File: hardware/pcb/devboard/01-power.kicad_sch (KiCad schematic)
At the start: 42 parts, among them J1 BATTERIE JST-PH, J2 BOUTON contact JST-PH, J3 BOUTON LED JST-PH, Q1 AO3401A, Q2 2N7002, Q3 2N7002, SW1 QON, U2 BQ25896RTW, U3 TPS63001DRCR, U4 TPS61023DRL

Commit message: feat(pcb): cost-optimize the dev board for JLCPCB
- shrink the outline to 99 x 45 mm and recenter MH2/MH4, keeping every
  dimension under 100 mm to dodge the large-board engineering fee
- reshape the In2.Cu +5V plane, restore the GND_surface pour, refill zones
- widen the main VBUS run to 1.2 mm, clearing the G2 thermal warning
- mark J1/J2/J3/J13 (JST-PH) and SW1 DNP: hand-soldered, so the board is
  all-SMD and skips the through-hole wave-solder fixture
- move R1/R10/R11/R26/R27 to Basic 0603 (150R/56k/7.5k), dropping three
  extended feeders; values and the 5V feedback ratio preserved
- swap D1 to the promotional SMF5.0A C19077497 (identical part, fee waived)
- gen_fab: J13 takes no JLCPCB rotation correction (verified in preview)

Co-Authored-By: Claude Opus 4.8 <noreply@anthropic.com>
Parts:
- D1: LCSC C284108 -> C19077497
- J1, J2, J3, SW1: now not fitted
- R1: footprint Resistor_SMD:R_0402_1005Metric -> Resistor_SMD:R_0603_1608Metric; LCSC C25082 -> C22808; MPN 0402WGF1500TCE -> 0603WAF1500T5E
- R10: footprint Resistor_SMD:R_0402_1005Metric -> Resistor_SMD:R_0603_1608Metric; LCSC C25796 -> C23206; MPN 0402WGF5602TCE -> 0603WAF5602T5E
- R11: footprint Resistor_SMD:R_0402_1005Metric -> Resistor_SMD:R_0603_1608Metric; LCSC C25918 -> C23234; MPN 0402WGF7501TCE -> 0603WAF7501T5E
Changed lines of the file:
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@@
 			)
 		)
-		(property "Footprint" "Resistor_SMD:R_0402_1005Metric"
+		(property "Footprint" "Resistor_SMD:R_0603_1608Metric"
 			(at 768.35 43.18000000000001 0)
 			(effects
@@
 			(hide yes)
 		)
-		(property "LCSC" "C25082"
+		(property "LCSC" "C22808"
 			(at 768.35 35.56 0)
 			(effects
@@
 			(hide yes)
 		)
-		(property "MPN" "0402WGF1500TCE"
+		(property "MPN" "0603WAF1500T5E"
 			(at 768.35 33.02000000000001 0)
 			(effects
@@
 		(in_bom yes)
 		(on_board yes)
-		(dnp no)
+		(dnp yes)
 		(fields_autoplaced yes)
 		(property "Reference" "SW1"
@@
 			(hide yes)
 		)
-		(property "LCSC" "C284108"
+		(property "LCSC" "C19077497"
 			(at 229.87 107.94999999999999 0)
 			(effects
@@
 		(in_bom yes)
 		(on_board yes)
-		(dnp no)
+		(dnp yes)
 		(fields_autoplaced yes)
 		(property "Reference" "J1"
@@
 			)
 		)
-		(property "Footprint" "Resistor_SMD:R_0402_1005Metric"
+		(property "Footprint" "Resistor_SMD:R_0603_1608Metric"
 			(at 63.5 180.34 0)
 			(effects
@@
 			(hide yes)
 		)
-		(property "LCSC" "C25796"
+		(property "LCSC" "C23206"
 			(at 63.5 172.72000000000003 0)
 			(effects
@@
 			(hide yes)
 		)
-		(property "MPN" "0402WGF5602TCE"
+		(property "MPN" "0603WAF5602T5E"
 			(at 63.5 170.18 0)
 			(effects
@@
 			)
 		)
-		(property "Footprint" "Resistor_SMD:R_0402_1005Metric"
+		(property "Footprint" "Resistor_SMD:R_0603_1608Metric"
 			(at 139.7 180.34 0)
 			(effects
@@
 			(hide yes)
 		)
-		(property "LCSC" "C25918"
+		(property "LCSC" "C23234"
 			(at 139.7 172.72000000000003 0)
 			(effects
@@
 			(hide yes)
 		)
-		(property "MPN" "0402WGF7501TCE"
+		(property "MPN" "0603WAF7501T5E"
 			(at 139.7 170.18 0)
 			(effects
@@
 		(in_bom yes)
 		(on_board yes)
-		(dnp no)
+		(dnp yes)
 		(fields_autoplaced yes)
 		(property "Reference" "J2"
@@
 		(in_bom yes)
 		(on_board yes)
-		(dnp no)
+		(dnp yes)
 		(fields_autoplaced yes)
 		(property "Reference" "J3"

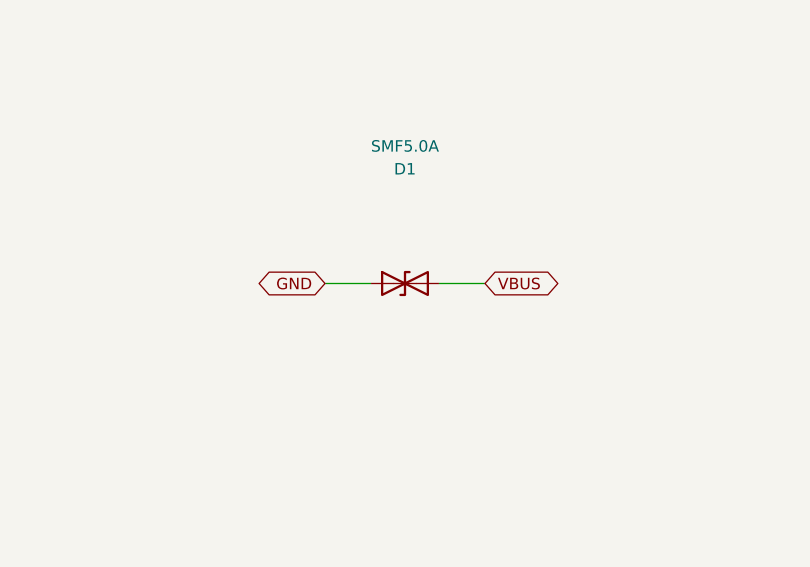
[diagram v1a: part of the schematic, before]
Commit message: fix(pcb): turn the VBUS TVS the right way round on both boards
D1 (SMF5.0A, unidirectional) carried Device:D_TVS, KiCad's bidirectional
symbol. Its pins are A1/A2, so no polarity is expressed, ERC has nothing to
reject, and the cathode landed wherever the wire ran — on GND. Plugging in
USB-C would have forward-biased the diode straight across VBUS, shorting the
port it protects.

Both boards now use Device:D_Zener, pin 1 = K, cathode on VBUS. The footprint
is rotated 180° so the symmetric SOD-123 pads keep the same copper: no track
moves, and DRC and unconnected counts are identical before and after.

check_pcb.py gains control H3 — every D<n> footprint must carry K/A pads. It
fails on the boards as they stood and passes 4/4 on the corrected ones.

Co-Authored-By: Claude Opus 5 (1M context) <noreply@anthropic.com>
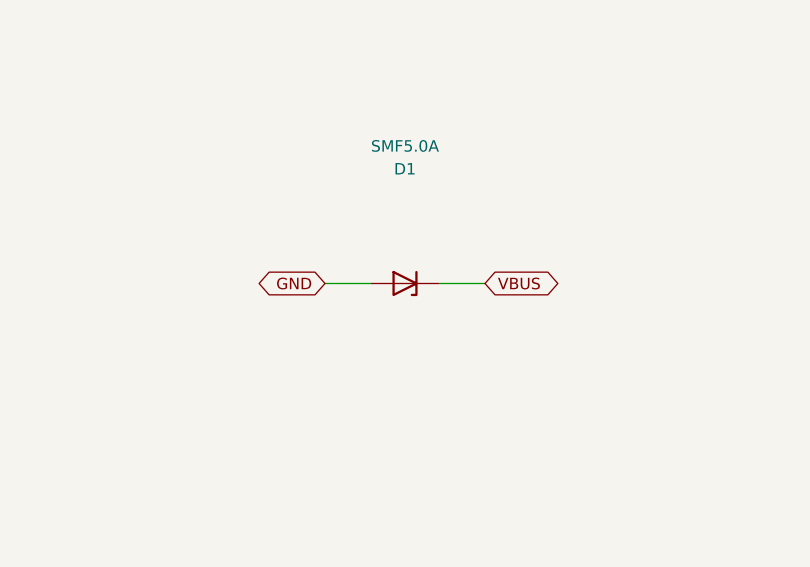
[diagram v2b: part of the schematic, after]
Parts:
- D1: symbol Device:D_TVS -> Device:D_Zener
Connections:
- net GND: now also D1.2 (A); no longer D1.1 (A1)
- net VBUS: now also D1.1 (K); no longer D1.2 (A2)
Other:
- moved on the sheet: D1
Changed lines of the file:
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@@
 	)
 	(symbol
-		(lib_id "Device:D_TVS")
-		(at 229.87 133.35 0)
+		(lib_id "Device:D_Zener")
+		(at 229.87 133.35 180)
 		(unit 1)
 		(exclude_from_sim no)
@@
 			(hide yes)
 		)
-		(property "Description" ""
+		(property "Description" "TVS unidirectionnelle 5 V. Symbole zener parce que Device:D_TVS est bidirectionnel : ses broches A1/A2 n'expriment aucune polarité, et rien alors n'empêche la cathode d'atterrir sur GND."
 			(at 229.87 110.49 0)
 			(effects
